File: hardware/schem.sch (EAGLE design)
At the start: 12 parts, among them IC1 7805L, Q1 IRF512, Q2 IRF512, Q5 IRF9530, Q6 IRF9530, U1 TINY45-20-DIP

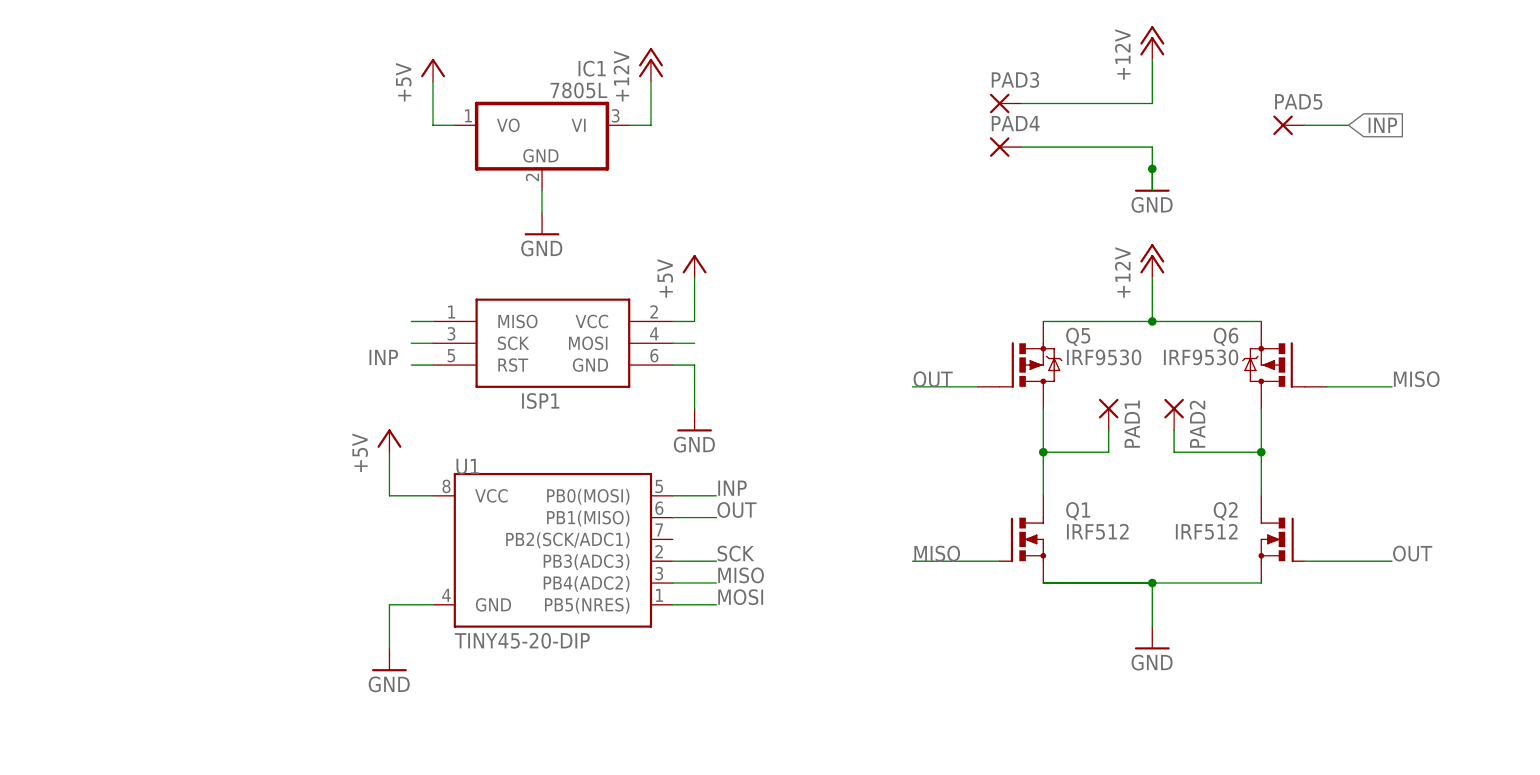
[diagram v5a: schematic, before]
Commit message: added large ground plane and power supply capacitors
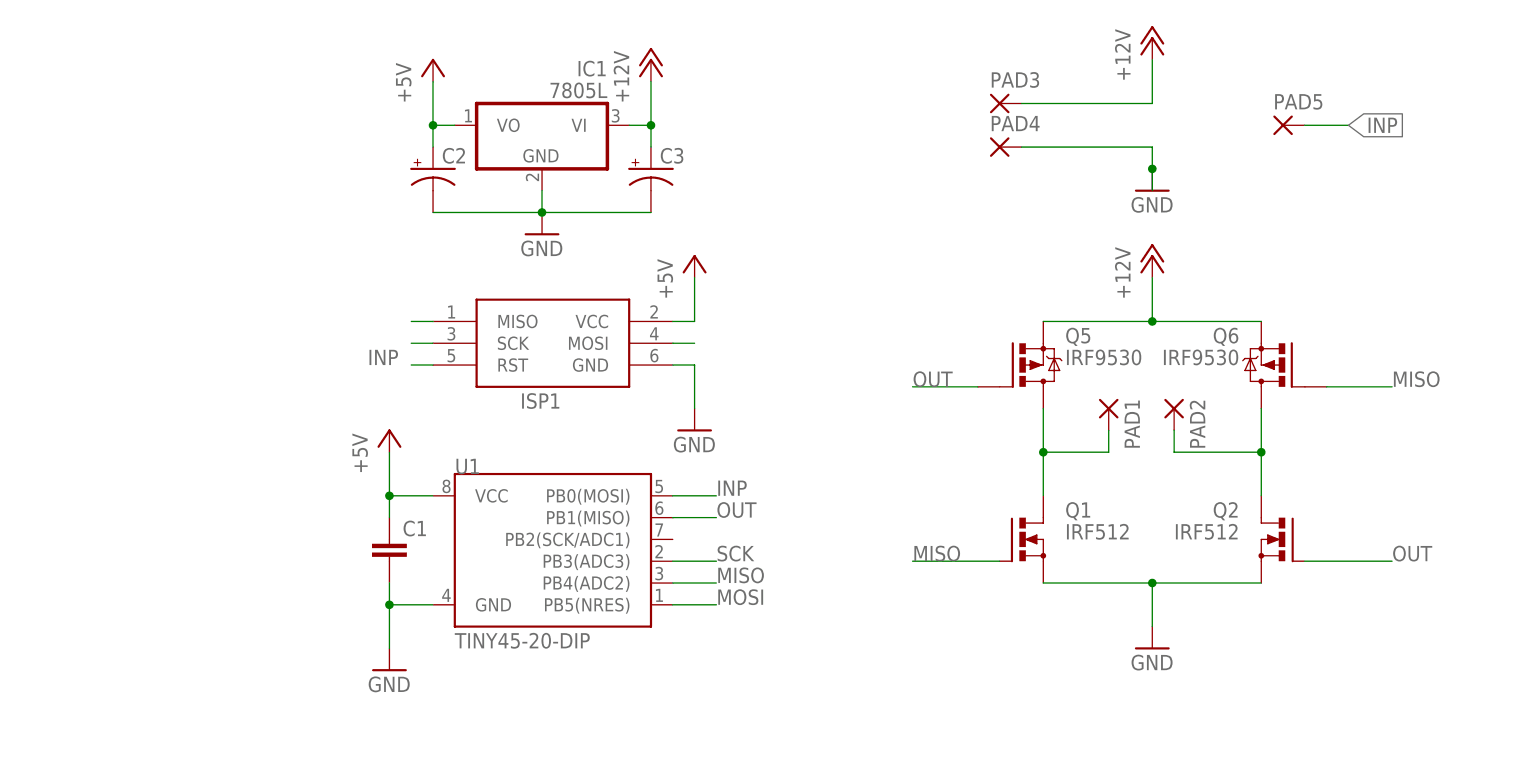
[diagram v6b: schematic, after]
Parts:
- added C1: (no value), rcl:C-EU025-025X050
- added C2, C3: (no value), rcl:CPOL-USE2.5-6
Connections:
- net +12V: now also C3.+
- net +5V: now also C1.1, C2.+
- net GND: now also C1.2, C2.-, C3.-
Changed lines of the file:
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@@
 <part name="Q1" library="transistor-power" deviceset="IRF512" device=""/>
 <part name="Q2" library="transistor-power" deviceset="IRF512" device=""/>
+<part name="C1" library="rcl" deviceset="C-EU" device="025-025X050"/>
+<part name="C2" library="rcl" deviceset="CPOL-US" device="E2.5-6"/>
+<part name="C3" library="rcl" deviceset="CPOL-US" device="E2.5-6"/>
 </parts>
 <sheets>
@@
 <instance part="Q1" gate="1" x="116.84" y="40.64"/>
 <instance part="Q2" gate="1" x="147.32" y="40.64" rot="MR0"/>
+<instance part="C1" gate="G$1" x="43.18" y="40.64"/>
+<instance part="C2" gate="G$1" x="48.26" y="83.82"/>
+<instance part="C3" gate="G$1" x="73.66" y="83.82"/>
 </instances>
 <busses>
@@
 <wire x1="73.66" y1="88.9" x2="73.66" y2="93.98" width="0.1524" layer="91"/>
 <pinref part="P+2" gate="1" pin="+12V"/>
+<pinref part="C3" gate="G$1" pin="+"/>
+<wire x1="73.66" y1="88.9" x2="73.66" y2="86.36" width="0.1524" layer="91"/>
+<junction x="73.66" y="88.9"/>
 </segment>
 <segment>
@@
 <wire x1="60.96" y1="81.28" x2="60.96" y2="78.74" width="0.1524" layer="91"/>
 <pinref part="GND2" gate="1" pin="GND"/>
+<pinref part="C3" gate="G$1" pin="-"/>
+<wire x1="73.66" y1="78.74" x2="60.96" y2="78.74" width="0.1524" layer="91"/>
+<junction x="60.96" y="78.74"/>
+<pinref part="C2" gate="G$1" pin="-"/>
+<wire x1="48.26" y1="78.74" x2="60.96" y2="78.74" width="0.1524" layer="91"/>
 </segment>
 <segment>
@@
 <pinref part="U1" gate="G$1" pin="GND"/>
 <wire x1="48.26" y1="33.02" x2="43.18" y2="33.02" width="0.1524" layer="91"/>
-</segment>
-<segment>
-<wire x1="144.78" y1="35.56" x2="132.08" y2="35.56" width="0.1524" layer="91"/>
+<pinref part="C1" gate="G$1" pin="2"/>
+<wire x1="43.18" y1="35.56" x2="43.18" y2="33.02" width="0.1524" layer="91"/>
+<junction x="43.18" y="33.02"/>
+</segment>
+<segment>
+<pinref part="Q1" gate="1" pin="S"/>
+<pinref part="Q2" gate="1" pin="S"/>
+<wire x1="119.38" y1="35.56" x2="132.08" y2="35.56" width="0.1524" layer="91"/>
 <pinref part="GND5" gate="1" pin="GND"/>
-<wire x1="132.08" y1="35.56" x2="119.38" y2="35.56" width="0.1524" layer="91"/>
+<wire x1="132.08" y1="35.56" x2="144.78" y2="35.56" width="0.1524" layer="91"/>
 <wire x1="132.08" y1="35.56" x2="132.08" y2="30.48" width="0.1524" layer="91"/>
 <junction x="132.08" y="35.56"/>
-<pinref part="Q1" gate="1" pin="S"/>
-<pinref part="Q2" gate="1" pin="S"/>
 </segment>
 </net>
@@
 <wire x1="48.26" y1="88.9" x2="48.26" y2="93.98" width="0.1524" layer="91"/>
 <pinref part="P+3" gate="1" pin="+5V"/>
+<pinref part="C2" gate="G$1" pin="+"/>
+<wire x1="48.26" y1="88.9" x2="48.26" y2="86.36" width="0.1524" layer="91"/>
+<junction x="48.26" y="88.9"/>
 </segment>
 <segment>
@@
 <pinref part="U1" gate="G$1" pin="VCC"/>
 <wire x1="48.26" y1="45.72" x2="43.18" y2="45.72" width="0.1524" layer="91"/>
+<pinref part="C1" gate="G$1" pin="1"/>
+<wire x1="43.18" y1="45.72" x2="43.18" y2="43.18" width="0.1524" layer="91"/>
+<junction x="43.18" y="45.72"/>
 </segment>
 </net>
@@
 </segment>
 </net>
-<net name="N$3" class="0">
-<segment>
-<wire x1="119.38" y1="35.56" x2="132.08" y2="35.56" width="0.1524" layer="91"/>
-</segment>
-</net>

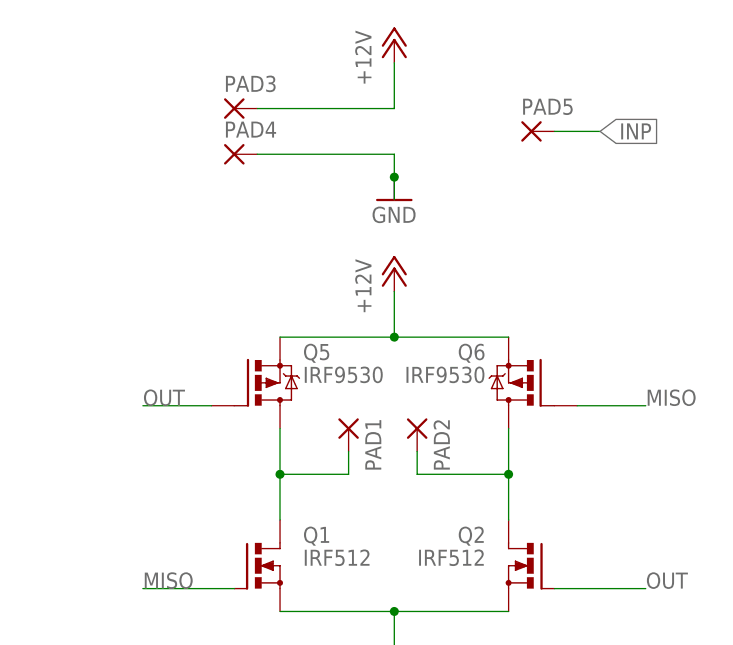
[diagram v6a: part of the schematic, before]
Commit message: modified silkscreen and worked on Power supply capacitor placement
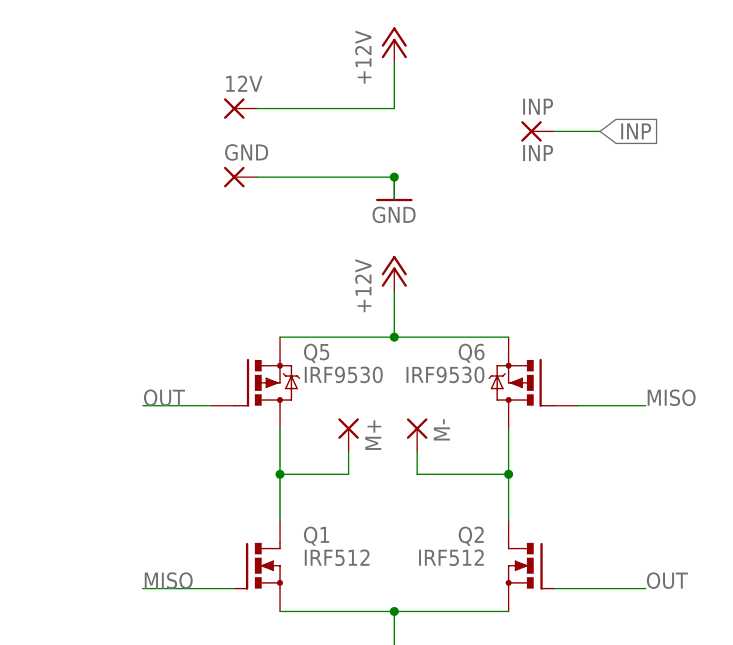
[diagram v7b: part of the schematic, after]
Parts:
- removed PAD4: (no value), wirepad:3,81/1,3
- added GND: (no value), wirepad:3,81/1,3
- INP: value (none) -> INP
- renumbered PAD1 to M+, PAD2 to M-, PAD3 to 12V, PAD5 to INP
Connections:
- net GND: now also GND.P; no longer PAD4.P
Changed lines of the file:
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@@
 <part name="GND5" library="supply1" deviceset="GND" device=""/>
 <part name="U1" library="SparkFun-DigitalIC" deviceset="ATTINY45" device="TINY45-20-DIP" value="TINY45-20-DIP"/>
-<part name="PAD3" library="wirepad" deviceset="3,81/1,3" device=""/>
-<part name="PAD4" library="wirepad" deviceset="3,81/1,3" device=""/>
-<part name="PAD5" library="wirepad" deviceset="2,15/1,0" device=""/>
-<part name="PAD1" library="wirepad" deviceset="3,81/1,3" device=""/>
-<part name="PAD2" library="wirepad" deviceset="3,81/1,3" device=""/>
+<part name="12V" library="wirepad" deviceset="3,81/1,3" device=""/>
+<part name="GND" library="wirepad" deviceset="3,81/1,3" device=""/>
+<part name="INP" library="wirepad" deviceset="2,15/1,0" device="" value="INP"/>
+<part name="M+" library="wirepad" deviceset="3,81/1,3" device=""/>
+<part name="M-" library="wirepad" deviceset="3,81/1,3" device=""/>
 <part name="Q5" library="transistor-power" deviceset="IRF9530" device=""/>
 <part name="Q6" library="transistor-power" deviceset="IRF9530" device=""/>
@@
 <instance part="GND5" gate="1" x="132.08" y="27.94"/>
 <instance part="U1" gate="G$1" x="63.5" y="38.1"/>
-<instance part="PAD3" gate="1" x="114.3" y="91.44"/>
-<instance part="PAD4" gate="1" x="114.3" y="86.36"/>
-<instance part="PAD5" gate="1" x="147.32" y="88.9"/>
-<instance part="PAD1" gate="1" x="127" y="55.88" rot="R270"/>
-<instance part="PAD2" gate="1" x="134.62" y="55.88" rot="R270"/>
+<instance part="12V" gate="1" x="114.3" y="91.44"/>
+<instance part="GND" gate="1" x="114.3" y="83.82"/>
+<instance part="INP" gate="1" x="147.32" y="88.9"/>
+<instance part="M+" gate="1" x="127" y="55.88" rot="R270"/>
+<instance part="M-" gate="1" x="134.62" y="55.88" rot="R270"/>
 <instance part="Q5" gate="G$1" x="116.84" y="60.96"/>
 <instance part="Q6" gate="G$1" x="147.32" y="60.96" rot="MR0"/>
@@
 <wire x1="119.38" y1="50.8" x2="127" y2="50.8" width="0.1524" layer="91"/>
 <wire x1="127" y1="50.8" x2="127" y2="53.34" width="0.1524" layer="91"/>
-<pinref part="PAD1" gate="1" pin="P"/>
+<pinref part="M+" gate="1" pin="P"/>
 <wire x1="119.38" y1="50.8" x2="119.38" y2="45.72" width="0.1524" layer="91"/>
 <junction x="119.38" y="50.8"/>
@@
 <wire x1="132.08" y1="91.44" x2="132.08" y2="96.52" width="0.1524" layer="91"/>
 <pinref part="P+1" gate="1" pin="+12V"/>
-<pinref part="PAD3" gate="1" pin="P"/>
+<pinref part="12V" gate="1" pin="P"/>
 <wire x1="116.84" y1="91.44" x2="132.08" y2="91.44" width="0.1524" layer="91"/>
 </segment>
@@
 <pinref part="GND1" gate="1" pin="GND"/>
 <wire x1="132.08" y1="83.82" x2="132.08" y2="81.28" width="0.1524" layer="91"/>
-<pinref part="PAD4" gate="1" pin="P"/>
-<wire x1="116.84" y1="86.36" x2="132.08" y2="86.36" width="0.1524" layer="91"/>
-<wire x1="132.08" y1="86.36" x2="132.08" y2="83.82" width="0.1524" layer="91"/>
+<pinref part="GND" gate="1" pin="P"/>
+<wire x1="116.84" y1="83.82" x2="132.08" y2="83.82" width="0.1524" layer="91"/>
 <junction x="132.08" y="83.82"/>
 </segment>
@@
 <wire x1="149.86" y1="88.9" x2="154.94" y2="88.9" width="0.1524" layer="91"/>
 <label x="154.94" y="88.9" size="1.778" layer="95" xref="yes"/>
-<pinref part="PAD5" gate="1" pin="P"/>
+<pinref part="INP" gate="1" pin="P"/>
 </segment>
 <segment>
@@
 <wire x1="134.62" y1="50.8" x2="144.78" y2="50.8" width="0.1524" layer="91"/>
 <junction x="144.78" y="50.8"/>
-<pinref part="PAD2" gate="1" pin="P"/>
+<pinref part="M-" gate="1" pin="P"/>
 <pinref part="Q6" gate="G$1" pin="D"/>
 <pinref part="Q2" gate="1" pin="D"/>

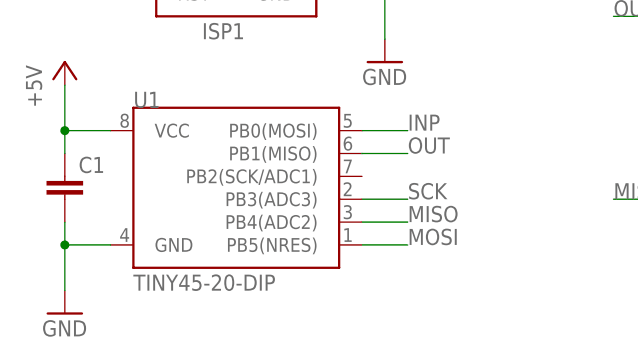
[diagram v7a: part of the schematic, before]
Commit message: modified silkscreen and worked on Power supply capacitor placement
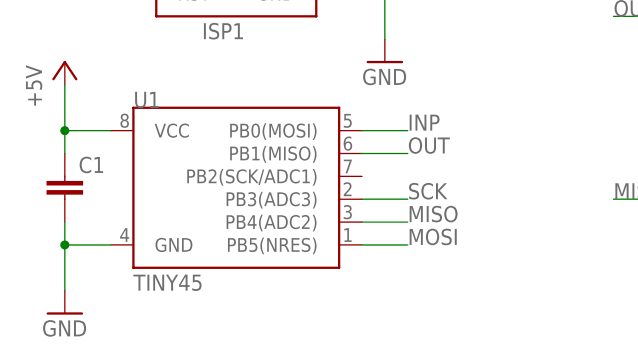
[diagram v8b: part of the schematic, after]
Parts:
- U1: value TINY45-20-DIP -> TINY45
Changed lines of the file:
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@@
 <part name="P+6" library="supply1" deviceset="+12V" device=""/>
 <part name="GND5" library="supply1" deviceset="GND" device=""/>
-<part name="U1" library="SparkFun-DigitalIC" deviceset="ATTINY45" device="TINY45-20-DIP" value="TINY45-20-DIP"/>
+<part name="U1" library="SparkFun-DigitalIC" deviceset="ATTINY45" device="TINY45-20-DIP" value="TINY45"/>
 <part name="12V" library="wirepad" deviceset="3,81/1,3" device=""/>
 <part name="GND" library="wirepad" deviceset="3,81/1,3" device=""/>
